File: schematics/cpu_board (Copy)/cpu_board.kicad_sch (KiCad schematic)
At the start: 69 parts, among them J600 Euro96pin, J601 clock, J602 clock1, J602_1 clock_dtack, J603 Conn_02x08_Counter_Clockwise, J604 systemTickFreq, J605 Conn_01x32, Q7 2N3904, Q8 2N3904, SW1 Reset, U1 MC68000FN, U600 68000D, U600rst1 ICM7555xB, U601 74LS393, U602 74HC164, U603 74HC14, U604 ATmega8-16P, U605 74LS20, U606 74HC4078, U607 74LS139

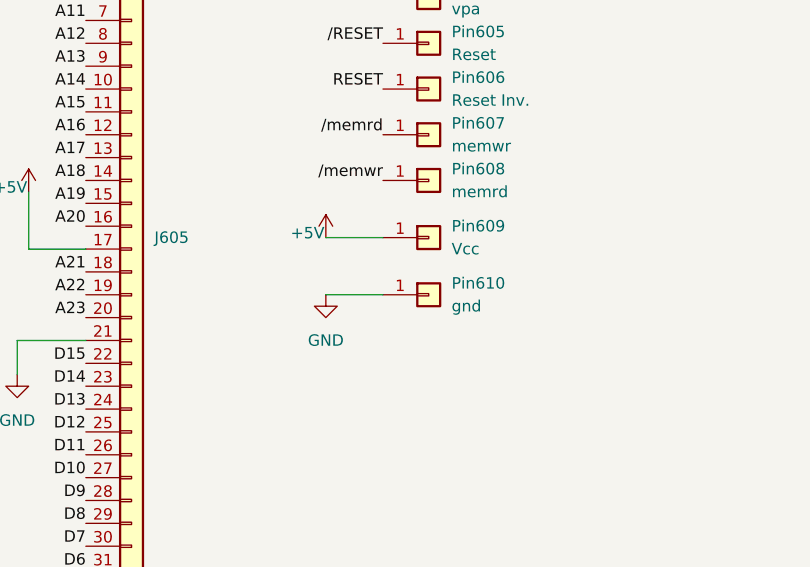
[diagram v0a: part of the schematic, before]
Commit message: PDS600 100% routed
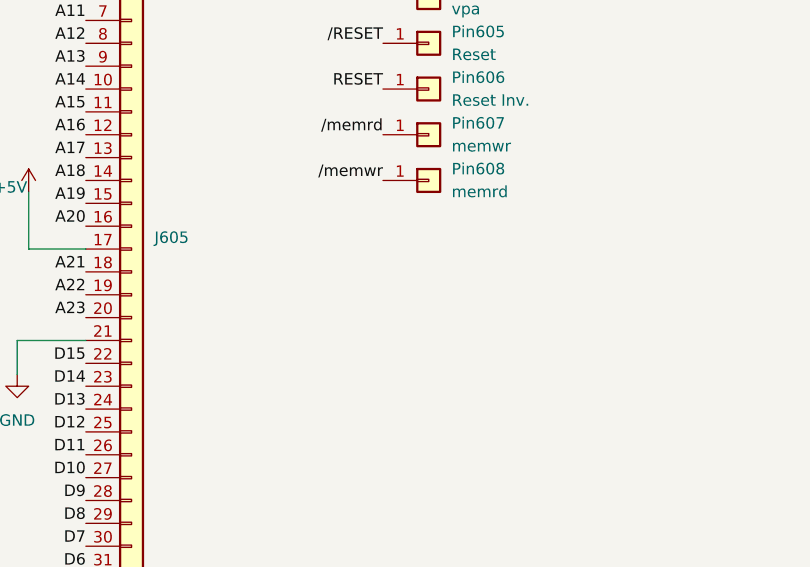
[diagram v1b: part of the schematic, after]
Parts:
- removed Pin609: Vcc, Connector_PinHeader_2.54mm:PinHeader_1x01_P2.54mm_Vertical, symbol Connector_Generic:Conn_01x01
- removed Pin610: gnd, Connector_PinHeader_2.54mm:PinHeader_1x01_P2.54mm_Vertical, symbol Connector_Generic:Conn_01x01
